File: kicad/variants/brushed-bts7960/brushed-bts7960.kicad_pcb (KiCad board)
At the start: 2 copper layers, 124.3 x 100.1 mm, 482 parts, among them IC1 rp2040_RP2040_breakout_swd, J1 HDR-M-2.54_1x3, J2 HDR-M-2.54_1x4, J3 HDR-M-2.54_1x4, J4 HDR-M-2.54_1x4, U1 SN74AHC244DW, U2 BTN7970, U3 BTN7970, U4 BTN7970, U5 BTN7970, U6 BMI160, U7 SPX3819M5-L-3-3/TR

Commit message: feat(kicad): доработка на плате, расширение до 180x100, альтернативный DC/DC
Перенос доработки из схемы на плату + PM2.

Плата выросла 124.51x100.33 -> 180.51x100.33 мм (+56 мм вправо).
Причина: снабберные резисторы 5 Вт выводные, шаг 30.5 мм, корпус 25x9 мм.
На старую плату они не помещались нигде — ближайшее свободное место было
в 48 мм от клемм мотора, что смысл снаббера убивает.

В новой полосе справа от клемм:

- M1: D1 вертикально у клемм, R27 вправо, C15 обратно влево (y 55..76);
- M2: то же для D2/R28/C16 (y 88..109);
- PM2 внизу (y 117..138).

Шины M+ и M- идут параллельно и не пересекаются: клемма -> супрессор ->
резистор -> плёнка -> обратно понизу к клемме.

На старой части платы: C10-C13 470 нФ слева от выводов драйверов (под
корпусом TO-263 места нет), пад GND заведён переходным на нижний полигон;
C14 1000 мкФ вверху, симметрично C9 — как на доработанной вручную плате.

PM2 — Mean Well NSD10-48S5 (22-72 В -> 5 В / 2 А), альтернатива PM1
SKMW30G-05, ставится один из двух. Отверстия свои, не общие с PM1:
геометрия падов совпадает (DIP-6, ряды 20.32 мм), но назначение выводов
расходится — у SKMW30G на выводе 3 плюс выхода, у NSD10 минус выхода, на
выводе 4 у одного TRIM, у другого плюс. Общая разводка закоротила бы
выход NSD10. Каждый модуль разведён по своему даташиту. Футпринт
Converter_DCDC_MeanWell_NSD10_THT из стандартной библиотеки KiCad.

Схема и плата сходятся: 69 компонентов с обеих сторон, все 58 цепей
совпадают по составу пинов. DRC без новых ошибок зазоров, замыканий и
пересечений — остаток тот же, что был после импорта (переходные массивы
в courtyard драйверов, шелкография EasyEDA, пады 0805/0603 без пасты).

Не разведено, 6 связей: VIN у C10-C12 (прямая трасса к выводу 7 режет
веер сигнальных выводов 2-6, нужен обход низом), +5V и SW у PM2,
островок GND у вывода 1 U4.

Co-Authored-By: Claude Opus 5 <noreply@anthropic.com>
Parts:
- added C10: 470n, C0805, F.Cu at (176.1, 61.8)
- added C11: 470n, C0805, F.Cu at (175.8, 88.3)
- added C12: 470n, C0805, F.Cu at (175.9, 113.2)
- added C13: 470n, C0805, F.Cu at (177.8, 141.6)
- added C14: 1000u, CAP-TH_BD16.0-P7.50-D0.8-FD-H25.0, F.Cu at (168.4, 60.4)
- added C15: 100n 100V, C_Rect_L10.0mm_W5.0mm_P5.00mm_P7.50mm, F.Cu at (256.0, 66.0)
- added C16: 100n 100V, C_Rect_L10.0mm_W5.0mm_P5.00mm_P7.50mm, F.Cu at (256.0, 98.8)
- added D1: 1.5KE30CA, D_DO-201AE_P15.24mm_Horizontal, F.Cu at (220.0, 57.0)
- added D2: 1.5KE30CA, D_DO-201AE_P15.24mm_Horizontal, F.Cu at (220.0, 89.8)
- added PM2: NSD10-48S5, Converter_DCDC_MeanWell_NSD10_THT, F.Cu at (242.0, 130.0)
- added R27: 22R 5W, R_Axial_Power_L25.0mm_W9.0mm_P30.48mm, F.Cu at (225.5, 57.0)
- added R28: 22R 5W, R_Axial_Power_L25.0mm_W9.0mm_P30.48mm, F.Cu at (225.5, 89.8)
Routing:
- net M2-: track 52.0 -> 113.2 mm
- net M1-: track 40.8 -> 101.6 mm
- net VIN: track 138.5 -> 182.5 mm
- net GND: track 199.7 -> 237.5 mm, vias 8 -> 12
- net M2+: track 41.4 -> 62.8 mm
- net M1+: track 28.4 -> 49.7 mm
- net M2_SNUB: track 0.00 -> 9.00 mm
- net M1_SNUB: track 0.00 -> 9.00 mm
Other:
- board size 124.3 x 100.1 mm -> 180.3 x 100.1 mm

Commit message: feat(kicad): стекап 2 oz, сплошная земля драйверов, расчёт силовых цепей
Расчёт по геометрии платы (новый scripts/pcb_power_check.py) и правки по
его результатам. Разбор — analysis/M1-driver-failure.md §7.

Что показал расчёт:

- Волновое сопротивление для этой платы не критерий: 36-126 Ом по
  ширинам, для 50 Ом нужна дорожка 2.7 мм. При ШИМ 20 кГц, UART и I2C
  дорожки электрически короткие, отражений нет.
- Узкое место — токонесущая способность. Силовые выходы M+- разведены
  дорожкой 4.0 мм. По IPC-2221 на 2 oz это 20.9 А при перегреве +45 C,
  то есть ровно номинал MY1016Z (21 А) без запаса на пуск (50-80 А).
  Держит это нижний полигон плюс 400 переходных под табами, но полигон
  разрезан сигнальными трассами (п. 3.4).
- Переходные по земле драйвера: ~1.15 мОм ствол, три параллельно
  0.38 мОм, при 20 А это 8 мВ и 0.15 Вт. Поправка к п. 3.4: по чистому
  сопротивлению это немного, узкое место — тепловые спицы 0.6 мм.

Правки на плате:

- Стекап задан явно: медь 70 мкм (2 oz) на обоих слоях, FR-4 1.51 мм,
  ENIG. Плата и так делается на 2 oz, но в файле была только общая
  толщина 1.6 мм — вес меди оставался догадкой, и расчёт по геометрии
  висел в воздухе. Теперь pcb_power_check.py берёт медь из проекта.
- Силовым выводам U2-U5 (1 GND, 7 VS, таб) и клеммам VIN/GND/M+- задано
  сплошное подключение к полигону вместо тепловых спиц.
- У вывода 1 каждого драйвера добавлены переходные GND: было 3 на
  драйвер, стало 5-6, с дорожкой 0.6 мм к паду. Всего переходных GND 22.
  Это то, что п. 5 «Следующая ревизия» просил как «6-10 переходов».

DRC: starved_thermal 7 -> 2 (оставшиеся у IC1, не силовые), висящих
переходных нет, новых замыканий и нарушений зазоров нет. Неразведённых
по-прежнему 6 — те же, что требуют ручной трассировки.

Расчёт не покрывает ток в полигонах (нужен полевой решатель, у KiCad
его нет) и сопротивление тепловых спиц. Проверять по-настоящему —
термопара и щупы под нагрузкой, п. 6.

Co-Authored-By: Claude Opus 5 <noreply@anthropic.com>
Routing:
- net GND: track 237.5 -> 257.4 mm, vias 12 -> 22
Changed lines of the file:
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@@
 	)
 	(setup
+		(stackup
+			(layer "F.SilkS"
+				(type "Top Silk Screen")
+			)
+			(layer "F.Paste"
+				(type "Top Solder Paste")
+			)
+			(layer "F.Mask"
+				(type "Top Solder Mask")
+				(thickness 0.01)
+			)
+			(layer "F.Cu"
+				(type "copper")
+				(thickness 0.07)
+			)
+			(layer "dielectric 1"
+				(type "core")
+				(thickness 1.51)
+				(material "FR4")
+				(epsilon_r 4.5)
+				(loss_tangent 0.02)
+			)
+			(layer "B.Cu"
+				(type "copper")
+				(thickness 0.07)
+			)
+			(layer "B.Mask"
+				(type "Bottom Solder Mask")
+				(thickness 0.01)
+			)
+			(layer "B.Paste"
+				(type "Bottom Solder Paste")
+			)
+			(layer "B.SilkS"
+				(type "Bottom Silk Screen")
+			)
+			(copper_finish "ENIG")
+			(dielectric_constraints no)
+		)
 		(pad_to_mask_clearance 0)
 		(allow_soldermask_bridges_in_footprints no)
@@
 			(solder_mask_margin 0.0508)
 			(solder_paste_margin 0)
+			(zone_connect 2)
 			(thermal_bridge_angle 0)
 		)
@@
 			(solder_mask_margin 0.0508)
 			(solder_paste_margin 0)
+			(zone_connect 2)
 			(thermal_bridge_angle 0)
 		)
@@
 			(solder_mask_margin 0.0508)
 			(solder_paste_margin 0)
+			(zone_connect 2)
 			(thermal_bridge_angle 0)
 		)
@@
 			(solder_mask_margin 0.0508)
 			(solder_paste_margin 0)
+			(zone_connect 2)
 			(thermal_bridge_angle 0)
 		)
@@
 			(solder_mask_margin 0.0508)
 			(solder_paste_margin 0)
+			(zone_connect 2)
 			(thermal_bridge_angle 0)
 		)
@@
 			(solder_mask_margin 0.0508)
 			(solder_paste_margin 0)
+			(zone_connect 2)
 			(thermal_bridge_angle 0)
 		)
@@
 			(solder_mask_margin 0.0508)
 			(solder_paste_margin 0)
+			(zone_connect 2)
 			(thermal_bridge_angle 0)
 		)
@@
 			(solder_mask_margin 0.0508)
 			(solder_paste_margin 0)
+			(zone_connect 2)
 			(thermal_bridge_angle 0)
 		)
@@
 			(solder_mask_margin 0.0508)
 			(solder_paste_margin 0)
+			(zone_connect 2)
 			(thermal_bridge_angle 0)
 		)
@@
 			(solder_mask_margin 0.0508)
 			(solder_paste_margin 0)
+			(zone_connect 2)
 			(thermal_bridge_angle 0)
 		)
@@
 			(solder_mask_margin 0.0508)
 			(solder_paste_margin 0)
+			(zone_connect 2)
 			(thermal_bridge_angle 0)
 		)
@@
 			(solder_mask_margin 0.0508)
 			(solder_paste_margin 0)
+			(zone_connect 2)
 			(thermal_bridge_angle 0)
 		)
@@
 			(solder_mask_margin 0.0508)
 			(solder_paste_margin 0)
+			(zone_connect 2)
 			(thermal_bridge_angle 0)
 		)
@@
 			(solder_mask_margin 0.0508)
 			(solder_paste_margin 0)
+			(zone_connect 2)
 			(thermal_bridge_angle 0)
 		)
@@
 			(solder_mask_margin 0.0508)
 			(solder_paste_margin 0)
+			(zone_connect 2)
 			(thermal_bridge_angle 0)
 		)
@@
 			(solder_mask_margin 0.0508)
 			(solder_paste_margin 0)
+			(zone_connect 2)
 			(thermal_bridge_angle 0)
 		)
@@
 			(solder_mask_margin 0.0508)
 			(solder_paste_margin 0)
+			(zone_connect 2)
 			(thermal_bridge_angle 0)
 		)
@@
 			(solder_mask_margin 0.0508)
 			(solder_paste_margin 0)
+			(zone_connect 2)
 			(thermal_bridge_angle 0)
 		)
@@
 	)
 	(segment
+		(start 181.186 132.931)
+		(end 180.119 131.173)
+		(width 0.6)
+		(layer "F.Cu")
+		(net "GND")
+	)
+	(segment
 		(start 127.4726 86.1874)
 		(end 128.227 86.1874)
@@
 	)
 	(segment
+		(start 181.44 108.293)
+		(end 181.419 106.473)
+		(width 0.6)
+		(layer "F.Cu")
+		(net "GND")
+	)
+	(segment
 		(start 152.611 113.754)
 		(end 152.865 113.5)
@@
 	)
 	(segment
+		(start 181.313 58.89)
+		(end 179.219 58.873)
+		(width 0.6)
+		(layer "F.Cu")
+		(net "GND")
+	)
+	(segment
 		(start 141.181 97.768)
 		(end 143.721 97.768)
@@
 	)
 	(segment
+		(start 181.44 108.293)
+		(end 182.519 106.473)
+		(width 0.6)
+		(layer "F.Cu")
+		(net "GND")
+	)
+	(segment
 		(start 161.12 130.899)
 		(end 162.4502 132.2292)
@@
 	)
 	(segment
+		(start 181.3552 83.528)
+		(end 180.219 81.773)
+		(width 0.6)
+		(layer "F.Cu")
+		(net "GND")
+	)
+	(segment
 		(start 161.12 116.421)
 		(end 160.739 116.04)
@@
 	)
 	(segment
+		(start 181.3552 83.528)
+		(end 182.419 81.773)
+		(width 0.6)
+		(layer "F.Cu")
+		(net "GND")
+	)
+	(segment
+		(start 181.44 108.293)
+		(end 179.319 108.273)
+		(width 0.6)
+		(layer "F.Cu")
+		(net "GND")
+	)
+	(segment
 		(start 129.497 94.069)
 		(end 129.497 92.575)
@@
 	)
 	(segment
+		(start 181.186 132.931)
+		(end 179.119 132.973)
+		(width 0.6)
+		(layer "F.Cu")
+		(net "GND")
+	)
+	(segment
 		(start 161.12 106.261)
 		(end 161.12 111.087)
@@
 	)
 	(segment
+		(start 181.3552 83.528)
+		(end 181.319 81.773)
+		(width 0.6)
+		(layer "F.Cu")
+		(net "GND")
+	)
+	(segment
 		(start 175.82 87.27)
 		(end 176.819 87.273)
@@
 	)
 	(segment
+		(start 181.186 132.931)
+		(end 181.219 131.173)
+		(width 0.6)
+		(layer "F.Cu")
+		(net "GND")
+	)
+	(segment
 		(start 98.89 74.13)
 		(end 101.43 74.13)
@@
 	)
 	(via
+		(at 179.219 58.873)
+		(size 0.61)
+		(drill 0.305)
+		(layers "F.Cu" "B.Cu")
+		(net "GND")
+	)
+	(via
+		(at 181.219 131.173)
+		(size 0.61)
+		(drill 0.305)
+		(layers "F.Cu" "B.Cu")
+		(net "GND")
+	)
+	(via
+		(at 180.119 131.173)
+		(size 0.61)
+		(drill 0.305)
+		(layers "F.Cu" "B.Cu")
+		(net "GND")
+	)
+	(via
+		(at 179.119 132.973)
+		(size 0.61)
+		(drill 0.305)
+		(layers "F.Cu" "B.Cu")
+		(net "GND")
+	)
+	(via
 		(at 134.196 97.752)
 		(size 0.61)
@@
 	)
 	(via
+		(at 181.319 81.773)
+		(size 0.61)
+		(drill 0.305)
+		(layers "F.Cu" "B.Cu")
+		(net "GND")
+	)
+	(via
 		(at 176.919 112.173)
 		(size 0.61)
@@
 	)
 	(via
+		(at 180.219 81.773)
+		(size 0.61)
+		(drill 0.305)
+		(layers "F.Cu" "B.Cu")
+		(net "GND")
+	)
+	(via
 		(at 152.611 113.754)
 		(size 0.62)
@@
 	)
 	(via
+		(at 182.419 81.773)
+		(size 0.61)
+		(drill 0.305)
+		(layers "F.Cu" "B.Cu")
+		(net "GND")
+	)
+	(via
+		(at 182.519 106.473)
+		(size 0.61)
+		(drill 0.305)
+		(layers "F.Cu" "B.Cu")
+		(net "GND")
+	)
+	(via
+		(at 181.419 106.473)
+		(size 0.61)
+		(drill 0.305)
+		(layers "F.Cu" "B.Cu")
+		(net "GND")
+	)
+	(via
 		(at 148.928 113.754)
 		(size 0.62)
@@
 		(size 0.61)
 		(drill 0.305)
+		(layers "F.Cu" "B.Cu")
+		(net "GND")
+	)
+	(via
+		(at 179.319 108.273)
+		(size 0.61)
+		(drill 0.305)

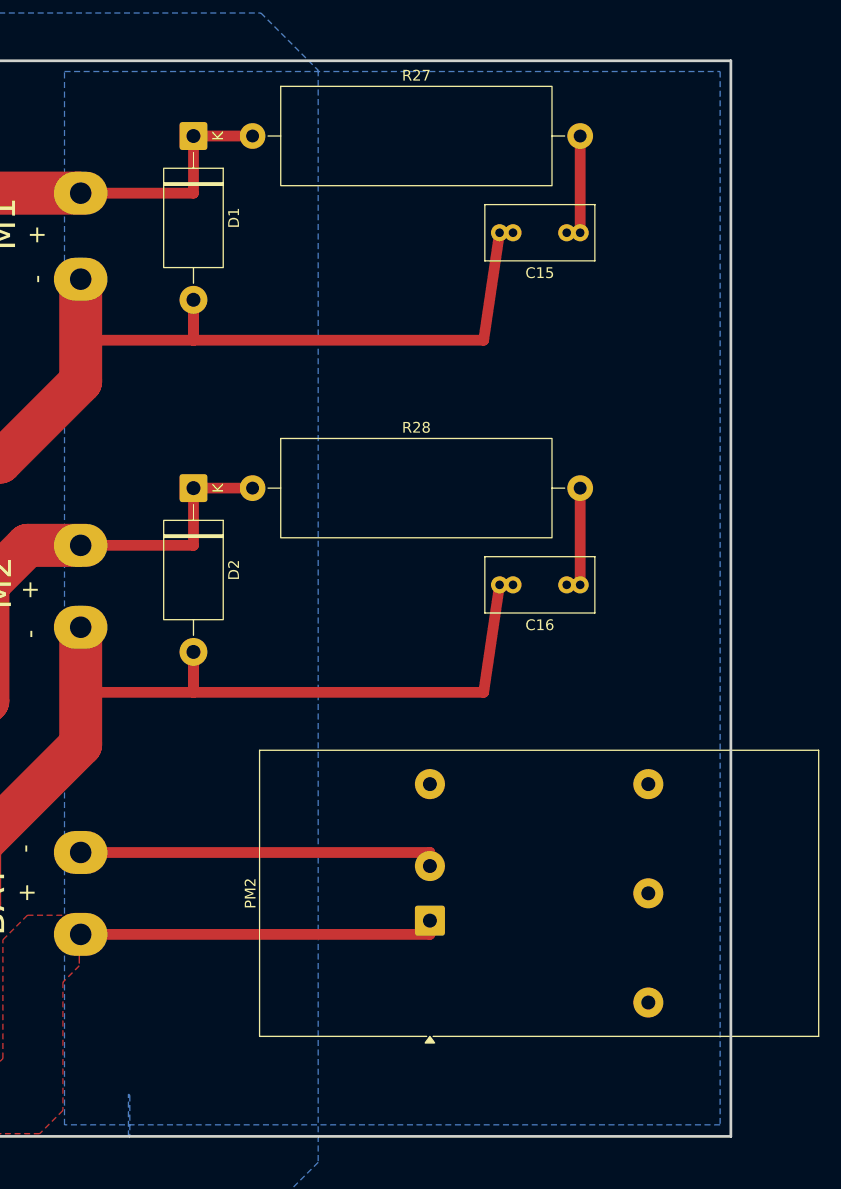
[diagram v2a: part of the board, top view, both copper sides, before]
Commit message: fix(kicad): резисторы вертикально, PM2 в габарите платы и разведён по питанию
По правкам с эскиза:

- R27/R28 развёрнуты на 90 градусов. Правая полоса перестроена в три
  вертикальные колонки: супрессор у клемм (x~216), мощный резистор
  (x~226), плёнка (x~236).
- PM2 сдвинут влево, в x 240..267. В прошлой раскладке он стоял у правого
  края и его корпус (52.4 мм при рядах выводов 20.32) вылезал за контур
  платы на 8 мм: пады были внутри, тело — нет. Этого я в прошлый раз не
  заметил.
- PM2 разведён по питанию: VIN на вывод 1, GND на выводы 2 и 3, трассами
  от силовых клемм.

Попутно вычищены остатки прежней раскладки: фильтр удаления старых
дорожек требовал, чтобы ОБА конца были в полосе, поэтому трассы,
упиравшиеся одним концом в клемму (x=209.51), пережили перекладку и
висели. Удалены, группы M1/M2 разведены заново.

+5V и SW у PM2 по-прежнему не разведены, и это осознанно. Поиск пути по
нижнему слою их находит (158 и 191 мм с обходами), но два таких выреза
разрезают GND-полигон надвое — в DRC появляются изолированные островки
GND и лишние starved_thermal. Это ровно дефект из §3.4 анализа, ради
которого всё и затевалось. Нужно решение по компоновке, а не слепая
трассировка.

DRC: 575 нарушений, все — исходные категории (переходные массивы в
courtyard драйверов, шелкография EasyEDA, пады без пасты, расхождение с
библиотекой). Ни замыканий, ни пересечений, ни висящих дорожек и
переходных, ни пересечения зон. Неразведённых 6.

Co-Authored-By: Claude Opus 5 <noreply@anthropic.com>
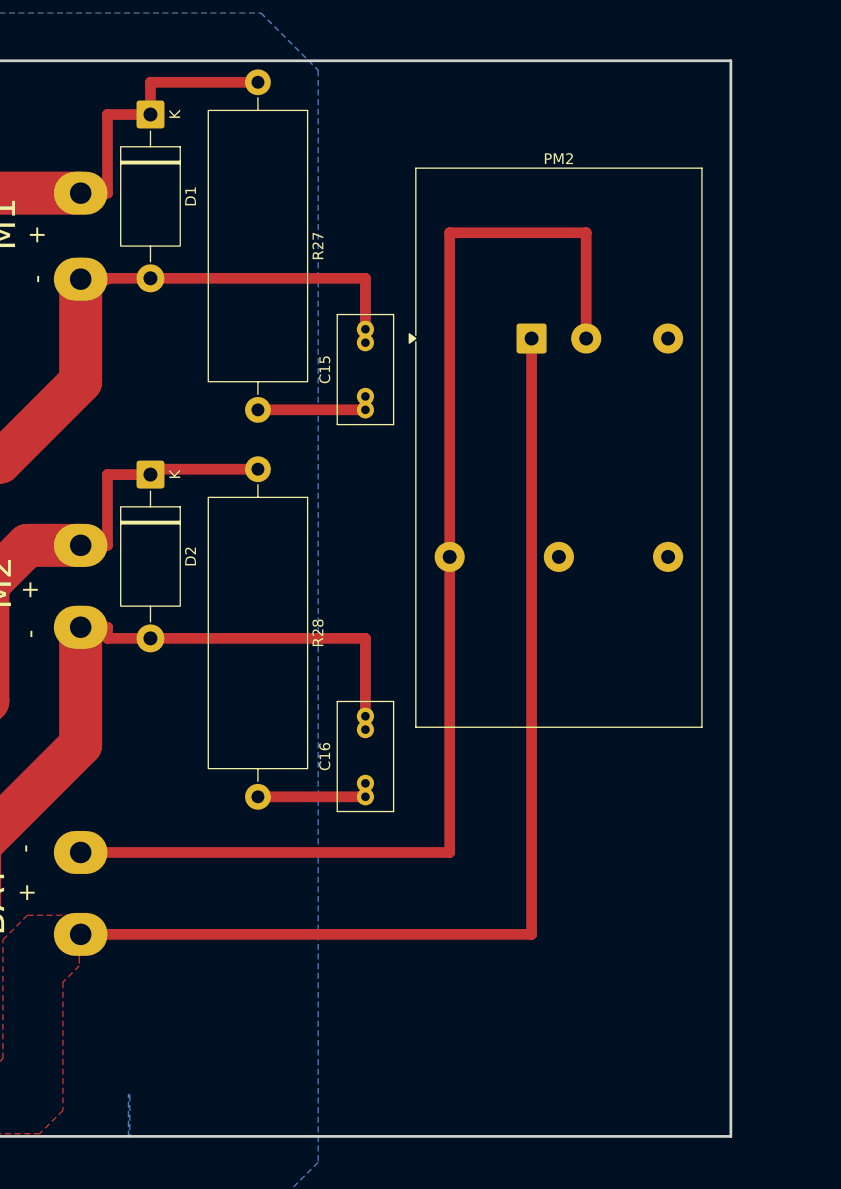
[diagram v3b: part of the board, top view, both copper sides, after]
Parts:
- moved PM2 55.0 mm to (251.5, 75.8), turned to 0 degrees
- moved C16 28.1 mm to (236.0, 118.5), turned to 90 degrees
- moved C15 25.9 mm to (236.0, 82.5), turned to 90 degrees
- moved R27 5.02 mm to (226.0, 52.0), turned to -90 degrees
- moved D1 4.47 mm to (216.0, 55.0)
- moved D2 4.19 mm to (216.0, 88.5)
- moved R28 1.83 mm to (226.0, 88.0), turned to -90 degrees
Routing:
- net GND: track 257.4 -> 338.2 mm
- net VIN: track 182.5 -> 246.1 mm
- net M1-: track 101.6 -> 73.3 mm
- net M2-: track 113.2 -> 88.0 mm
- net M1+: track 49.7 -> 55.2 mm
- net M2+: track 62.8 -> 65.0 mm
- net M2_SNUB: track 9.00 -> 10.0 mm
- net M1_SNUB: track 9.00 -> 10.0 mm
